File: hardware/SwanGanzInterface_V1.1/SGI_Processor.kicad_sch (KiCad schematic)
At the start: 24 parts, among them J2 Conn_01x08_Pin, SW2 MODE, SW3 ENTER, U4 LP-MSPM0G3507, U5 AdaFruit_1590, U7 FT232R

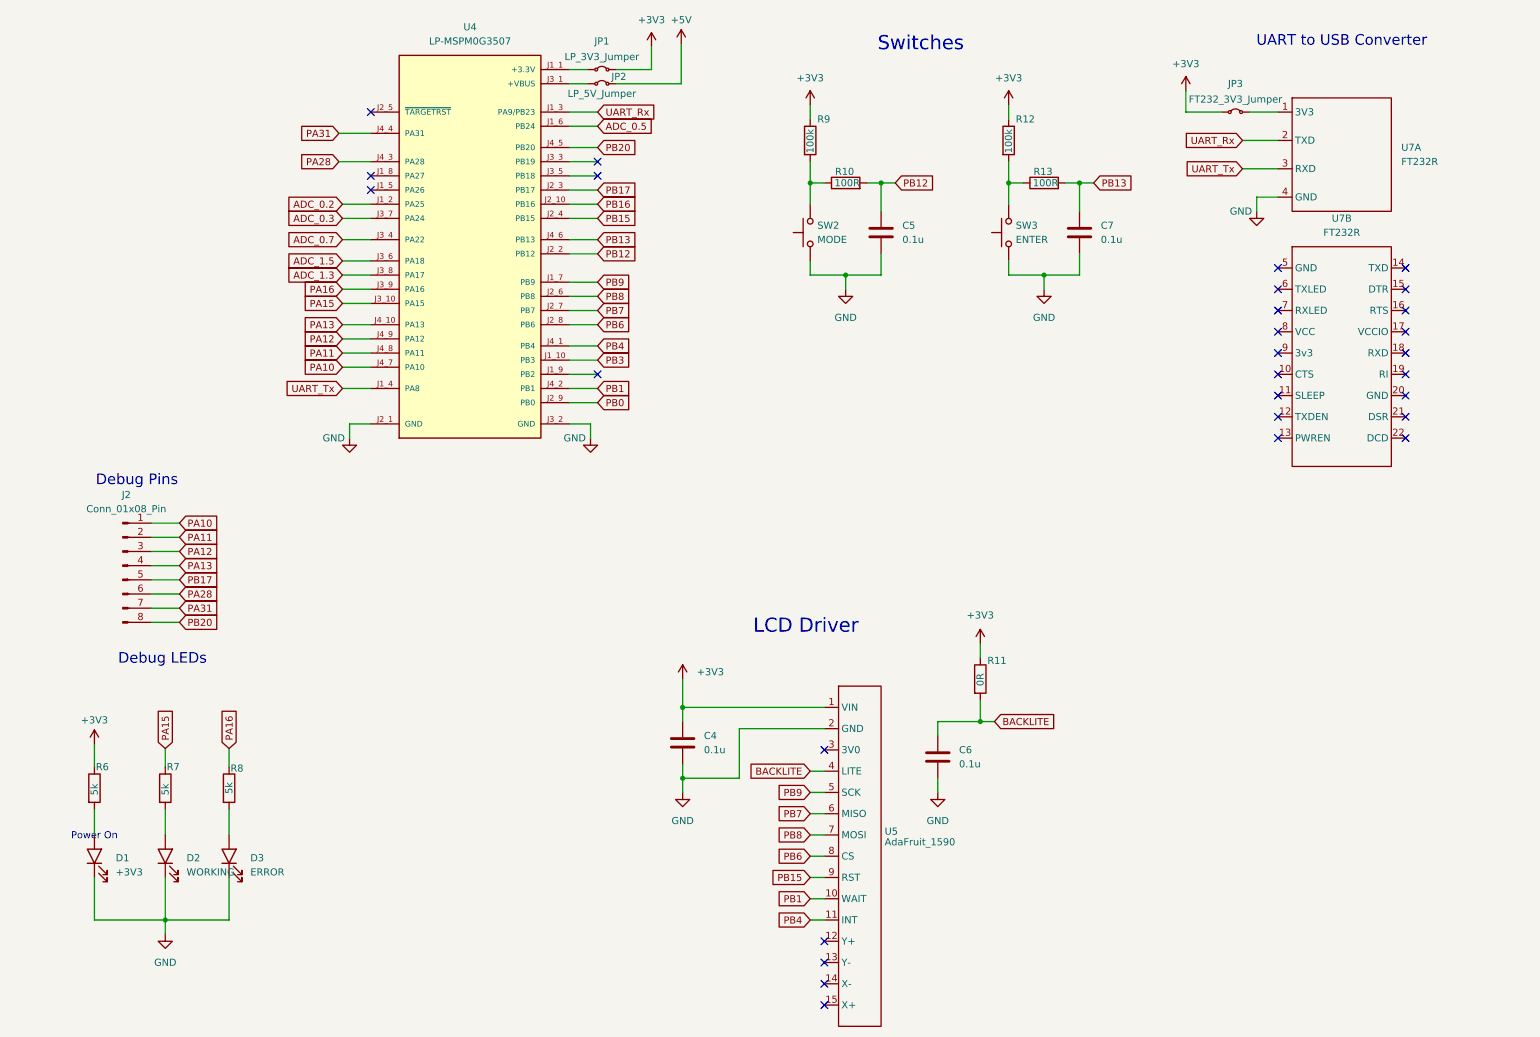
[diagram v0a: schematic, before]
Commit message: Pin Allocation, updated schematic with new pins, reassigned
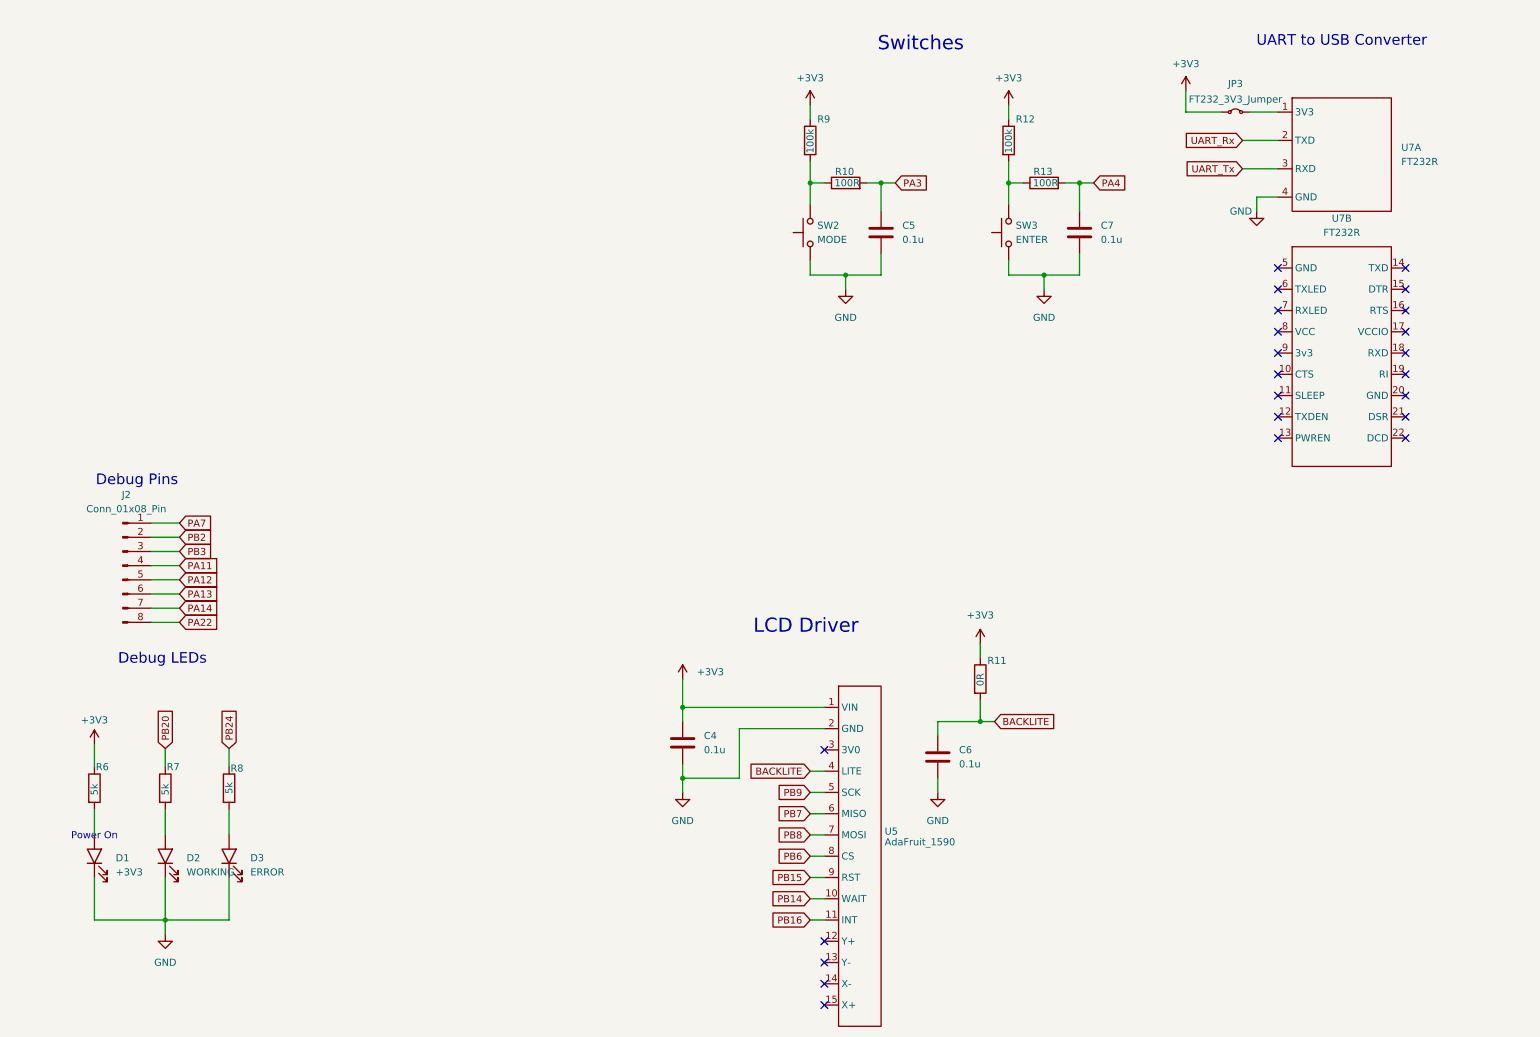
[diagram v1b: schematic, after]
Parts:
- removed JP1: LP_3V3_Jumper, SGI_FootprintsLib:PinHeader_1x02_P2.54mm_Vertical, symbol Jumper:Jumper_2_Small_Bridged
- removed JP2: LP_5V_Jumper, SGI_FootprintsLib:PinHeader_1x02_P2.54mm_Vertical, symbol Jumper:Jumper_2_Small_Bridged
- removed U4: LP-MSPM0G3507, SGI_FootprintsLib:ti_LP_MSPM0G3507, symbol SGI_SymbolLib:LP-MSPM0G3507
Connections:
- net PA15 is gone; now on net PB20: R7.1
- net PA28 is gone; now on net PA13: J2.6 (Pin_6)
- net PB17 is gone; now on net PA12: J2.5 (Pin_5)
- net PB4 is gone; now on net PB16: U5.11 (INT)
- net PA11: now also J2.4 (Pin_4); no longer J2.2 (Pin_2)
- net PA12: no longer J2.3 (Pin_3)
- net PA13: no longer J2.4 (Pin_4)
- net PB20: no longer J2.8 (Pin_8)
- net PB3: now also J2.3 (Pin_3)
- net PA10 renamed PA7
- net PA16 renamed PB24
- net PA31 renamed PA14
- net PB1 renamed PB14
- net PB12 renamed PA3
- net PB13 renamed PA4
- new net PA22: J2.8 (Pin_8)
- new net PB2: J2.2 (Pin_2)
- no-connect marks 29 -> 23

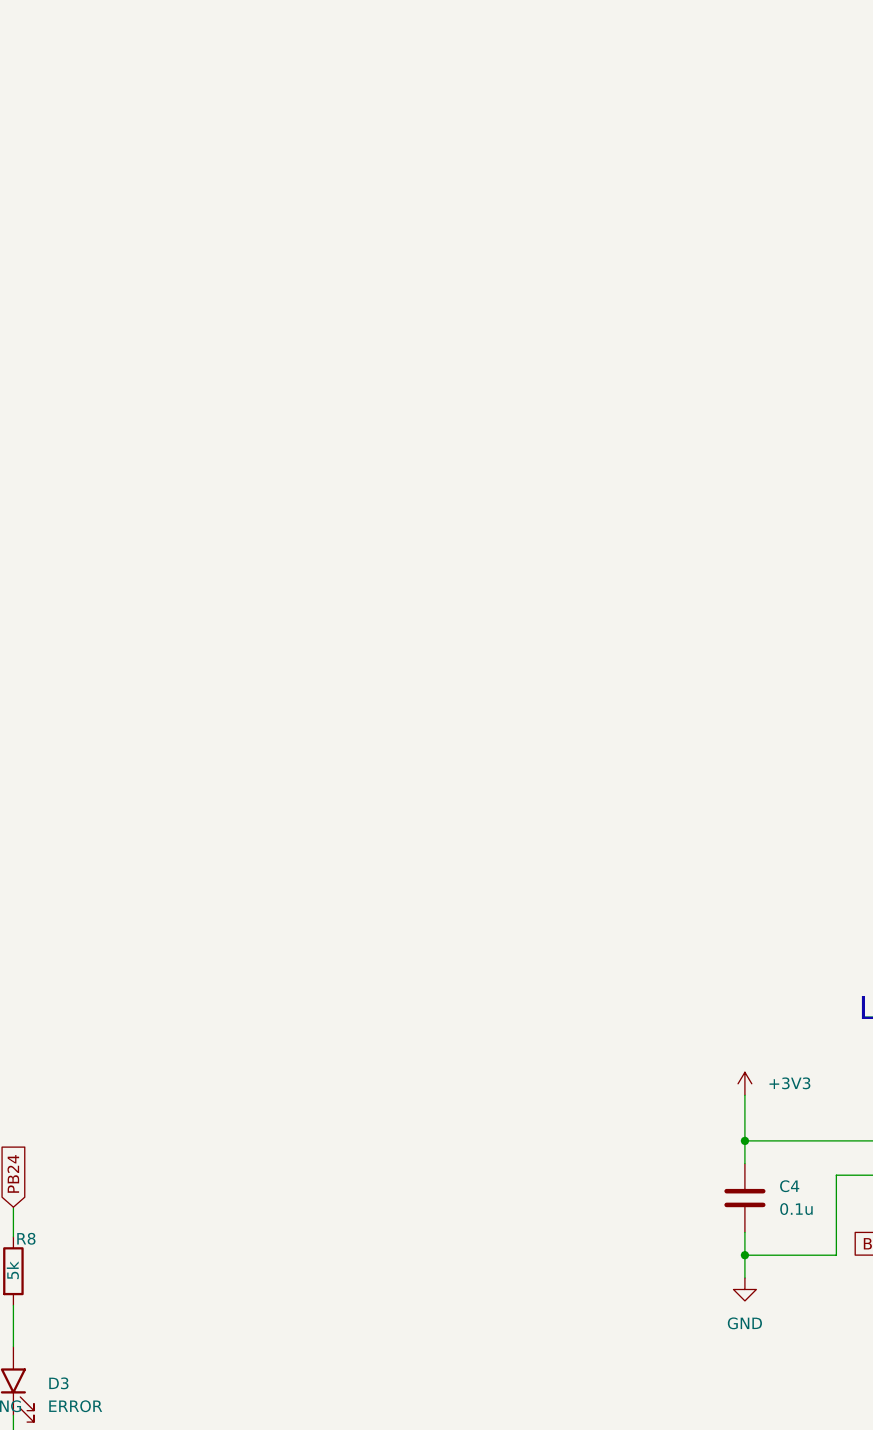
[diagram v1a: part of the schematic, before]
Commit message: Added MSP symbol/footprint
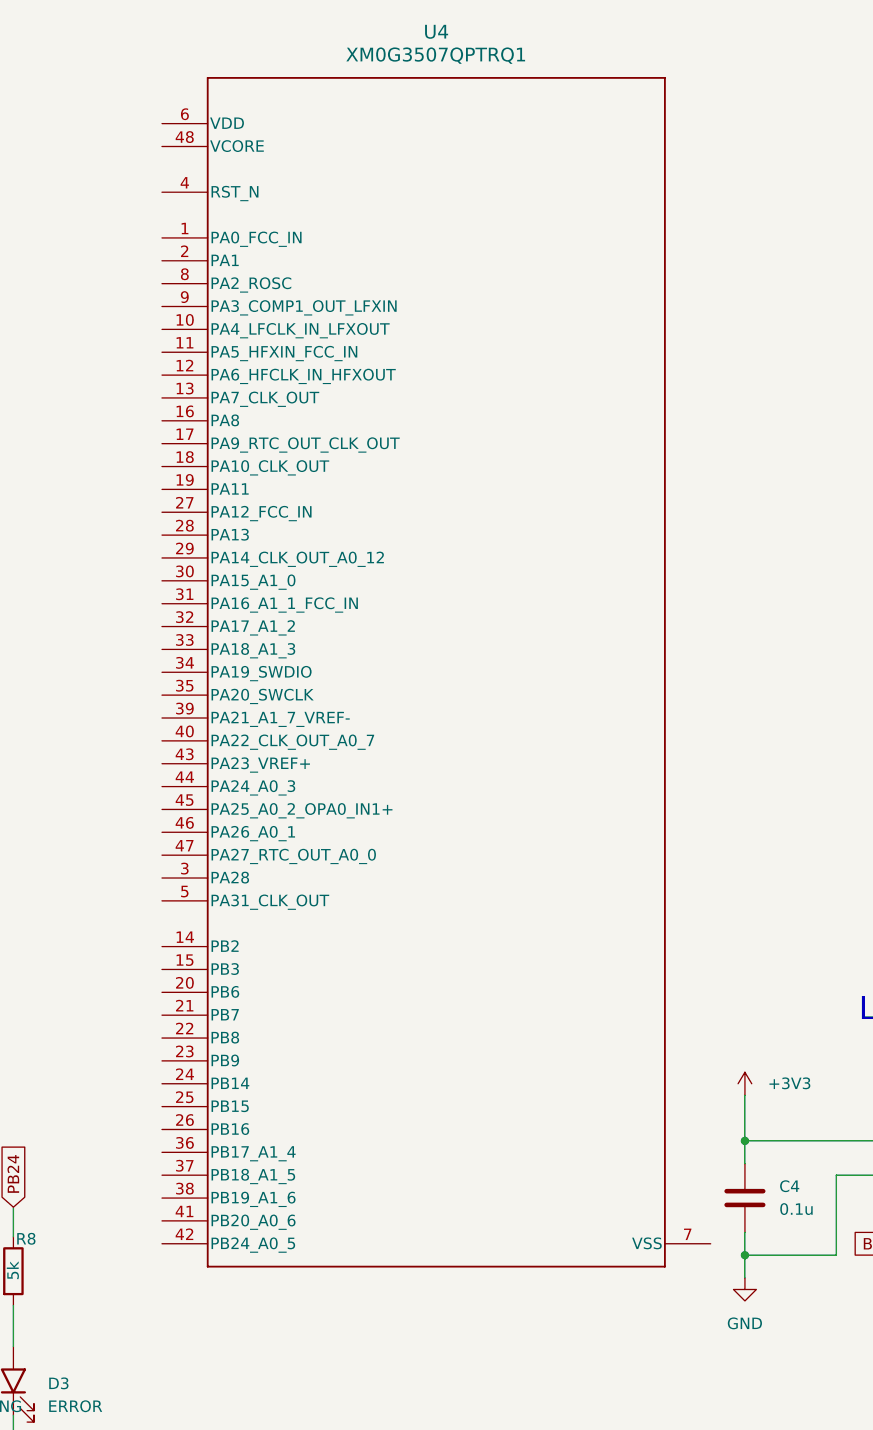
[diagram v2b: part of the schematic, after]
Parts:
- added U4: XM0G3507QPTRQ1, SGI_FootprintsLib:MSPM0_PT0048A-IPC_A, symbol SGI_SymbolLib:XM0G3507QPTRQ1
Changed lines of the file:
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@@
+	)
+	(symbol
+		(lib_id "SGI_SymbolLib:XM0G3507QPTRQ1")
+		(at 68.58 25.4 0)
+		(unit 1)
+		(exclude_from_sim no)
+		(in_bom yes)
+		(on_board yes)
+		(dnp no)
+		(fields_autoplaced yes)
+		(property "Reference" "U4"
+			(at 99.06 15.24 0)
+			(effects
+				(font
+					(size 1.524 1.524)
+				)
+			)
+		)
+		(property "Value" "XM0G3507QPTRQ1"
+			(at 99.06 17.78 0)
+			(effects
+				(font
+					(size 1.524 1.524)
+				)
+			)
+		)
+		(property "Footprint" "SGI_FootprintsLib:MSPM0_PT0048A-IPC_A"
+			(at 68.58 25.4 0)
+			(effects
+				(font
+					(size 1.27 1.27)
+					(italic yes)
+				)
+				(hide yes)
+			)
+		)
+		(property "Datasheet" "https://www.ti.com/lit/gpn/mspm0g3507-q1"
+			(at 68.58 25.4 0)
+			(effects
+				(font
+					(size 1.27 1.27)
+					(italic yes)
+				)
+				(hide yes)
+			)
+		)
+		(property "Description" ""
+			(at 68.58 25.4 0)
+			(effects
+				(font
+					(size 1.27 1.27)
+				)
+				(hide yes)
+			)
+		)
+		(pin "3"
+		)
+		(pin "27"
+		)
+		(pin "40"
+		)
+		(pin "12"
+		)
+		(pin "16"
+		)
+		(pin "28"
+		)
+		(pin "13"
+		)
+		(pin "45"
+		)
+		(pin "46"
+		)
+		(pin "10"
+		)
+		(pin "30"
+		)
+		(pin "31"
+		)
+		(pin "29"
+		)
+		(pin "18"
+		)
+		(pin "19"
+		)
+		(pin "11"
+		)
+		(pin "32"
+		)
+		(pin "33"
+		)
+		(pin "34"
+		)
+		(pin "39"
+		)
+		(pin "17"
+		)
+		(pin "44"
+		)
+		(pin "35"
+		)
+		(pin "47"
+		)
+		(pin "43"
+		)
+		(pin "26"
+		)
+		(pin "7"
+		)
+		(pin "24"
+		)
+		(pin "21"
+		)
+		(pin "25"
+		)
+		(pin "42"
+		)
+		(pin "23"
+		)
+		(pin "20"
+		)
+		(pin "14"
+		)
+		(pin "36"
+		)
+		(pin "37"
+		)
+		(pin "38"
+		)
+		(pin "41"
+		)
+		(pin "15"
+		)
+		(pin "22"
+		)
+		(pin "5"
+		)
+		(pin "6"
+		)
+		(pin "1"
+		)
+		(pin "2"
+		)
+		(pin "8"
+		)
+		(pin "9"
+		)
+		(pin "48"
+		)
+		(pin "4"
+		)
+		(instances
+			(project ""
+				(path "/4e9a6e30-f660-472b-9696-bea1f34b4545/b7986f9d-7bcd-462e-9f66-fb6deb5be406"
+					(reference "U4")
+					(unit 1)
+				)
+			)
+		)
 	)
 	(symbol

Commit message: Hooked up MSP
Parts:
- removed JP3: FT232_3V3_Jumper, SGI_FootprintsLib:PinHeader_1x02_P2.54mm_Vertical, symbol Jumper:Jumper_2_Small_Bridged
- removed U7: FT232R, SGI_FootprintsLib:FT232R-Breakout, symbol SGI_SymbolLib:FT232R-Breakout
- added C22: 10u, symbol Device:C
- added C23, C24: 1u, symbol Device:C
- added C8: 0.01u, Capacitor_SMD:C_0603_1608Metric, symbol Device:C
- added C9: 0.47u, symbol Device:C
- added R38: 47k, Resistor_SMD:R_0603_1608Metric, symbol Device:R
- added R40: 100k, symbol Device:R
- added SW4: MODE, SGI_FootprintsLib:SW_PUSH_6mm, symbol SGI_SymbolLib:SW_Push
- added Y1: ABM8AIG-40.000MHZ-12-2Z-T3, SGI_FootprintsLib:ABM8AIG25000MHZ122ZT3, symbol SGI_SymbolLib:ABM8AIG-40.000MHZ-12-2Z-T3
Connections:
- net PA11 is gone; now on net DEBUG4_PA11: J2.4 (Pin_4)
- net PA12 is gone; now on net DEBUG5_PA12: J2.5 (Pin_5)
- net PA13 is gone; now on net DEBUG6_PA13: J2.6 (Pin_6)
- net PA14 is gone; now on net DEBUG7_PA14: J2.7 (Pin_7)
- net PA22 is gone; now on net DEBUG8_PA22: J2.8 (Pin_8)
- net PA7 is gone; now on net DEBUG1_PA7: J2.1 (Pin_1)
- net PB14 is gone; now on net LCD_WAIT_PB14: U5.10 (WAIT)
- net PB15 is gone; now on net LCD_RST_PB15: U5.9 (RST)
- net PB16 is gone; now on net LCD_INT_PB16: U5.11 (INT)
- net PB2 is gone; now on net DEBUG2_PB2: J2.2 (Pin_2)
- net PB3 is gone; now on net DEBUG3_PB3: J2.3 (Pin_3)
- net PB6 is gone; now on net LCD_CS_PB6: U5.8 (CS)
- net PB7 is gone; now on net LCD_POCI_PB7: U5.6 (MISO)
- net PB8 is gone; now on net LCD_PICO_PB8: U5.7 (MOSI)
- net PB9 is gone; now on net LCD_SCK_PB9: U5.5 (SCK)
- net +3V3: now also U4.6 (VDD), C22.1, C23.1, R38.1
- net GND: now also U4.39 (PA21_A1_7_VREF-), U4.7 (VSS), C22.2, C23.2, C24.2, C8.2, C9.2, R40.1, SW4.1, Y1.2 (GND_1), Y1.4 (GND_2)
- net PA3: now also U4.9 (PA3_COMP1_OUT_LFXIN)
- net PA4: now also U4.10 (PA4_LFCLK_IN_LFXOUT)
- net PB20: now also U4.41 (PB20_A0_6)
- net PB24: now also U4.42 (PB24_A0_5)
- net LCD_Y+_A0.1: now reaches U5.12 (Y+)
- net LCD_Y+_A0.1: now also U4.46 (PA26_A0_1)
- net LCD_Y-_A0.0: now reaches U5.13 (Y-)
- net LCD_Y-_A0.0: now also U4.47 (PA27_RTC_OUT_A0_0)
- net LCD_X-_A0.2: now reaches U5.14 (X-)
- net LCD_X-_A0.2: now also U4.45 (PA25_A0_2_OPA0_IN1+)
- net LCD_X+_A0.3: now reaches U5.15 (X+)
- net LCD_X+_A0.3: now also U4.44 (PA24_A0_3)
- net HFXIN: now reaches U4.11 (PA5_HFXIN_FCC_IN)
- net HFXIN: now also Y1.1 (X1)
- net HFXOUT: now reaches U4.12 (PA6_HFCLK_IN_HFXOUT)
- net HFXOUT: now also Y1.3 (X2)
- net DEBUG1_PA7: now reaches U4.13 (PA7_CLK_OUT)
- net DEBUG2_PB2: now reaches U4.14 (PB2)
- net DEBUG3_PB3: now reaches U4.15 (PB3)
- net UART_TX_PA8: now reaches U4.16 (PA8)
- net UART_RX_PA9: now reaches U4.17 (PA9_RTC_OUT_CLK_OUT)
- net USB_CONN_PA10: now reaches U4.18 (PA10_CLK_OUT)
- net DEBUG4_PA11: now reaches U4.19 (PA11)
- net LCD_CS_PB6: now reaches U4.20 (PB6)
- net LCD_POCI_PB7: now reaches U4.21 (PB7)
- net LCD_PICO_PB8: now reaches U4.22 (PB8)
- net LCD_SCK_PB9: now reaches U4.23 (PB9)
- net LCD_WAIT_PB14: now reaches U4.24 (PB14)
- net LCD_RST_PB15: now reaches U4.25 (PB15)
- net LCD_INT_PB16: now reaches U4.26 (PB16)
- net DEBUG5_PA12: now reaches U4.27 (PA12_FCC_IN)
- net DEBUG6_PA13: now reaches U4.28 (PA13)
- net DEBUG7_PA14: now reaches U4.29 (PA14_CLK_OUT_A0_12)
- net SPEAK_DAC: now reaches U4.30 (PA15_A1_0)
- net THERM_LG_ADC_1.1: now reaches U4.31 (PA16_A1_1_FCC_IN)
- net THERM__HG_ADC_1.2: now reaches U4.32 (PA17_A1_2)
- net P1_LG_ADC_1.3: now reaches U4.33 (PA18_A1_3)
- net SWDIO: now reaches U4.34 (PA19_SWDIO)
- net SWCLK: now reaches U4.35 (PA20_SWCLK)
- net P1_HG_ADC_1.4: now reaches U4.36 (PB17_A1_4)
- net P2_LG_ADC_1.5: now reaches U4.37 (PB18_A1_5)
- net P2_HG_ADC_1.6: now reaches U4.38 (PB19_A1_6)
- net MSP_NRST: now reaches U4.4 (RST_N)
- net MSP_NRST: now also C8.1, R38.2, SW4.2
- net DEBUG8_PA22: now reaches U4.40 (PA22_CLK_OUT_A0_7)
- net at U4.43 (PA23_VREF+): now also C24.1
- net at U4.48 (VCORE): now also C9.1
- net at U4.8 (PA2_ROSC): now also R40.2
- no-connect marks 23 -> 5
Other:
- note added: "+/-0.1%"
- note added: "Following Launchpad Circuit"
- note removed: "UART to USB Converter"
- moved on the sheet: C4, C5, C6, C7, J2, R10, R11, R12, R13, R9, SW2, SW3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
